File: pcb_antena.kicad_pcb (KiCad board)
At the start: 2 copper layers, 29 parts, among them J1 Screw_Terminal_01x02, J2 Screw_Terminal_01x02, J3 Screw_Terminal_01x02, U1 TL084, U2 TL082, U3 LM7818_TO220, U4 AD620

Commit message: Versión lista para imprimir
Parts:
- removed J3: Screw_Terminal_01x02, TerminalBlock_MetzConnect:TerminalBlock_MetzConnect_Type011_RT05502HBLC_1x02_P5.00mm_Horizontal
- added H1: MountingHole_2.2mm_M2_ISO7380_Pad, MountingHole:MountingHole_2.2mm_M2_ISO7380_Pad, F.Cu at (217.0, 54.0)
- added H2: MountingHole_2.2mm_M2_ISO7380_Pad, MountingHole:MountingHole_2.2mm_M2_ISO7380_Pad, F.Cu at (218.0, 126.0)
- added H3: MountingHole_2.2mm_M2_ISO7380_Pad, MountingHole:MountingHole_2.2mm_M2_ISO7380_Pad, F.Cu at (120.0, 126.0)
- added H4: MountingHole_2.2mm_M2_ISO7380_Pad, MountingHole:MountingHole_2.2mm_M2_ISO7380_Pad, F.Cu at (120.0, 54.0)
- added J4: SMA, Connector_Coaxial:SMA_Amphenol_132289_EdgeMount, B.Cu at (217.6, 82.0)
- added R13: 0, huellas_proyecto:R_Axial_DIN0207_L6.3mm_D2.5mm_P10.16mm_Horizontal-pad2mm, F.Cu at (138.9, 74.0)
- added R14: 0, huellas_proyecto:R_Axial_DIN0207_L6.3mm_D2.5mm_P10.16mm_Horizontal-pad2mm, F.Cu at (138.9, 88.0)
- C1, C5, C6, C9: footprint Capacitor_THT:CP_Radial_D10.0mm_P5.00mm -> huellas_proyecto:CP_Radial_D10.0mm_P5.00mm-pad2mm2
- C2, C3, C4, C7, C8: footprint Capacitor_THT:C_Disc_D5.1mm_W3.2mm_P5.00mm -> huellas_proyecto:C_Disc_D5.1mm_W3.2mm_P5.00mm-pad2mm
- J1: value Screw_Terminal_01x02 -> VC_24V
- J2: value Screw_Terminal_01x02 -> Ant
- R1, R10, R11, R12, R2, R5, R6, R7, R8, R9: footprint Resistor_THT:R_Axial_DIN0207_L6.3mm_D2.5mm_P10.16mm_Horizontal -> huellas_proyecto:R_Axial_DIN0207_L6.3mm_D2.5mm_P10.16mm_Horizontal-pad2mm
- R3, R4: footprint Resistor_THT:R_Axial_DIN0207_L6.3mm_D2.5mm_P10.16mm_Horizontal -> huellas_proyecto:R_Axial_DIN0207_L6.3mm_D2.5mm_P15.24mm_Horizontal-pad2mm
- RV1: footprint Potentiometer_THT:Potentiometer_Bourns_3296W_Vertical -> huellas_proyecto:Potentiometer_Bourns_3296W_Vertical-pad2mm
- U1: footprint Package_DIP:DIP-14_W7.62mm_LongPads -> huellas_proyecto:DIP-14_W7.62mm_LongPads-2mm
- U2, U4: footprint Package_DIP:DIP-8_W7.62mm_LongPads -> huellas_proyecto:DIP-8_W7.62mm_LongPads-pad2mm
- U3: footprint Package_TO_SOT_THT:TO-220-3_Horizontal_TabDown -> huellas_proyecto:TO-220-3_Vertical-pad2mm
- moved J2 100.3 mm to (123.1, 83.5), turned to 90 degrees
- moved U1 90.7 mm to (139.5, 84.8), turned to 90 degrees
- moved C7 67.7 mm to (162.5, 77.0)
- moved C5 66.4 mm to (139.5, 59.0), turned to 90 degrees
- moved C8 66.1 mm to (162.5, 85.0)
- moved C6 61.0 mm to (139.5, 110.2), turned to -90 degrees
- moved R6 54.8 mm to (137.0, 64.5), turned to 180 degrees
- moved RV1 52.8 mm to (188.2, 71.7), turned to 180 degrees
- moved R10 47.3 mm to (137.0, 104.6), turned to 180 degrees
- moved R7 45.3 mm to (152.2, 64.5), turned to 180 degrees
- moved R5 43.4 mm to (144.6, 70.5), turned to 180 degrees
- moved C1 42.6 mm to (215.0, 115.6), turned to -90 degrees
- moved R9 40.0 mm to (144.6, 98.6), turned to 180 degrees
- moved C4 39.4 mm to (183.6, 93.5), turned to -90 degrees
- moved U4 35.3 mm to (186.9, 76.9)
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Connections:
- C1 pad 1: Net-(J1-Pin_2) -> Net-(J1-Pin_1)
- C2 pad 1: Net-(J1-Pin_2) -> Net-(J1-Pin_1)
- C7 pad 1: Net-(U1B--) -> Net-(U1C--)
- C8 pad 1: Net-(U1C--) -> Net-(U1B--)
- J1 pad 1: GND -> Net-(J1-Pin_1)
- J1 pad 2: Net-(J1-Pin_2) -> GND
- R10 pad 2: Net-(U1C-+) -> Net-(R10-Pad2)
- R5 pad 2: Net-(U1B-+) -> Net-(R13-Pad1)
- R6 pad 2: Net-(U1B-+) -> Net-(R13-Pad1)
- R9 pad 2: Net-(U1C-+) -> Net-(R10-Pad2)
- U1 pad 1: Net-(U1C-+) -> Net-(R10-Pad2)
- U1 pad 14: Net-(U1B-+) -> Net-(R13-Pad1)
- U3 pad 1: Net-(J1-Pin_2) -> Net-(J1-Pin_1)
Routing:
- net Vq: track 0.00 -> 92.3 mm
- net Net-(J2-Pin_1): track 0.00 -> 49.3 mm
- net Net-(J2-Pin_2): track 0.00 -> 39.1 mm
- net GND: track 0.00 -> 32.5 mm, vias 0 -> 6
- net Net-(R10-Pad2): track 0.00 -> 29.3 mm
- net Net-(U2A-+): track 0.00 -> 25.0 mm
- net Net-(J1-Pin_1): track 0.00 -> 22.3 mm
- net Net-(R13-Pad1): track 0.00 -> 22.2 mm
- net Net-(U4-+): track 0.00 -> 20.7 mm
- net Net-(U4--): track 0.00 -> 20.4 mm
- net Net-(U1D-+): track 0.00 -> 19.8 mm
- net Net-(C6-Pad1): track 0.00 -> 12.2 mm
- net Net-(C5-Pad1): track 0.00 -> 12.1 mm
- net Net-(J4-In): track 0.00 -> 10.6 mm
- net Net-(U1C--): track 0.00 -> 10.4 mm
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- added copper zone on F.Cu, net GND
- added copper zone on B.Cu, net VCC
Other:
- board outline added: 105.4 x 79.2 mm

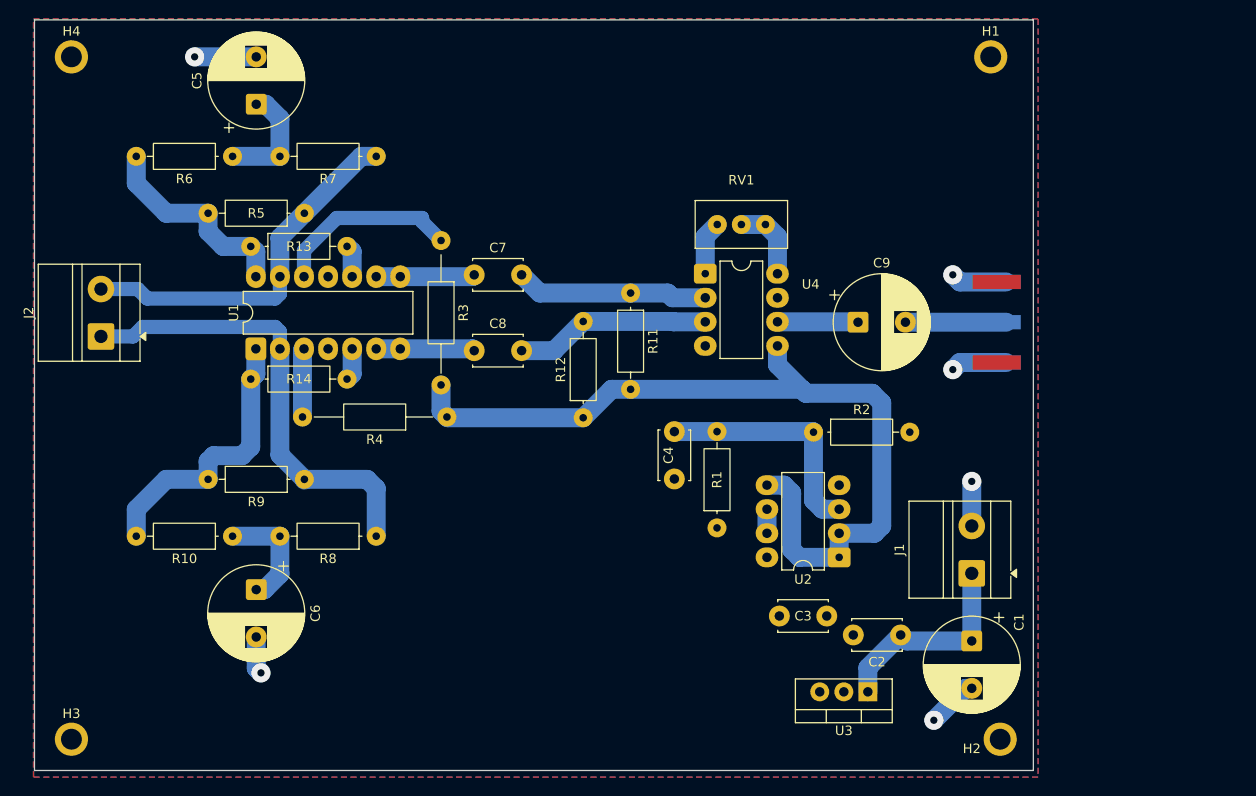
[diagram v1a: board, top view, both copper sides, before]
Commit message: Se agrego la otra placa en carpeta una nueva carpeta. Para revisión
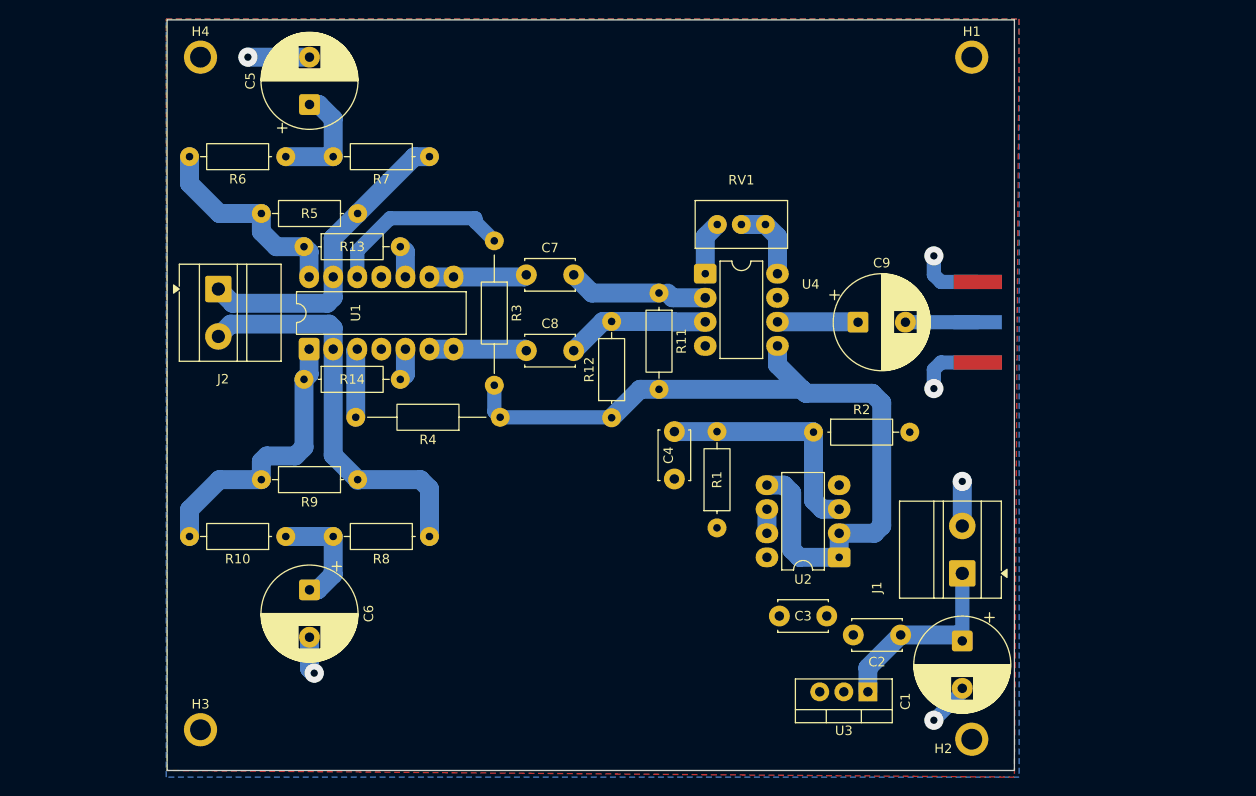
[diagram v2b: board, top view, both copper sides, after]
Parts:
- moved H3 13.7 mm to (133.6, 125.0)
- moved H4 13.6 mm to (133.6, 54.0)
- moved J2 13.4 mm to (135.5, 78.5), turned to -90 degrees
- moved C5 5.62 mm to (145.1, 59.0)
- moved C6 5.62 mm to (145.1, 110.2)
- moved R10 5.62 mm to (142.6, 104.6)
- moved R13 5.62 mm to (144.5, 74.0)
- moved R14 5.62 mm to (144.5, 88.0)
- moved R3 5.62 mm to (164.6, 73.4)
- moved R4 5.62 mm to (165.2, 92.0)
- moved R6 5.62 mm to (142.6, 64.5)
- moved R7 5.62 mm to (157.8, 64.5)
- moved R8 5.62 mm to (157.8, 104.6)
- moved U1 5.62 mm to (145.1, 84.8)
- moved R5 5.62 mm to (150.2, 70.5)
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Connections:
- R5 pad 1: Net-(J2-Pin_2) -> Net-(J2-Pin_1)
- R7 pad 1: Net-(J2-Pin_2) -> Net-(J2-Pin_1)
- R8 pad 1: Net-(J2-Pin_1) -> Net-(J2-Pin_2)
- R9 pad 1: Net-(J2-Pin_1) -> Net-(J2-Pin_2)
- U1 pad 13: Net-(J2-Pin_2) -> Net-(J2-Pin_1)
- U1 pad 2: Net-(J2-Pin_1) -> Net-(J2-Pin_2)
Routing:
- net Net-(J2-Pin_1): track 49.3 -> 33.0 mm
- net Net-(U4--): track 20.4 -> 14.0 mm
- net Vq: track 92.3 -> 86.6 mm
- net Net-(U4-+): track 20.7 -> 15.2 mm
- net Net-(J2-Pin_2): track 39.1 -> 43.0 mm
- net Net-(J4-In): track 10.6 -> 7.64 mm
- net GND: track 32.5 -> 33.7 mm
- net Net-(J1-Pin_1): track 22.3 -> 21.3 mm
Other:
- board size 105.4 x 79.2 mm -> 89.4 x 79.2 mm
